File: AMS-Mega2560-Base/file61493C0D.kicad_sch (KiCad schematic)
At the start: 40 parts, among them IC10 LM2597MX-ADJ_NOPB, IC11 LM2597M-3.3_NOPB, IC12 OPA2340PA, IC9 LM2670SX-5.0_NOPB, J21 Screw_Terminal_01x02, J22 Conn_01x06, Q6 IRF9Z34NPBF, U1 BK_HTC-15M, U2 TL431LP

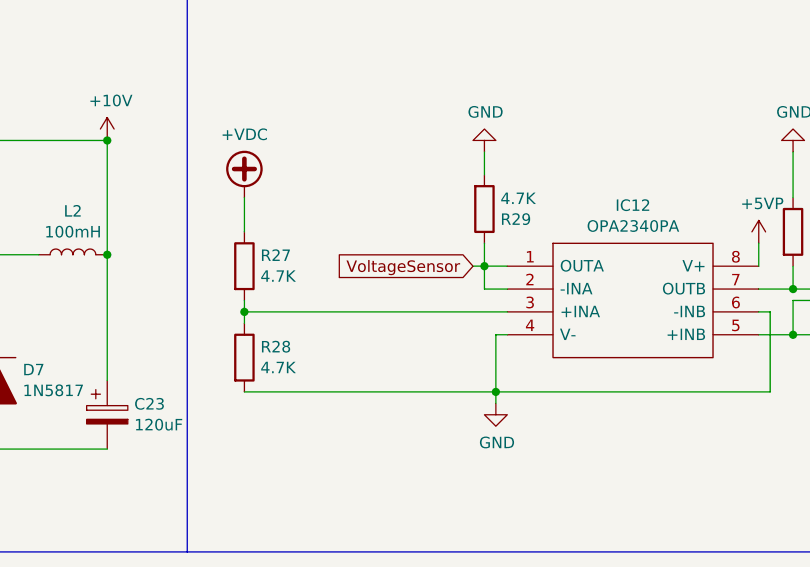
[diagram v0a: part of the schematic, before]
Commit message: slowly working on getting the board laid out and updates to some of the schematics.
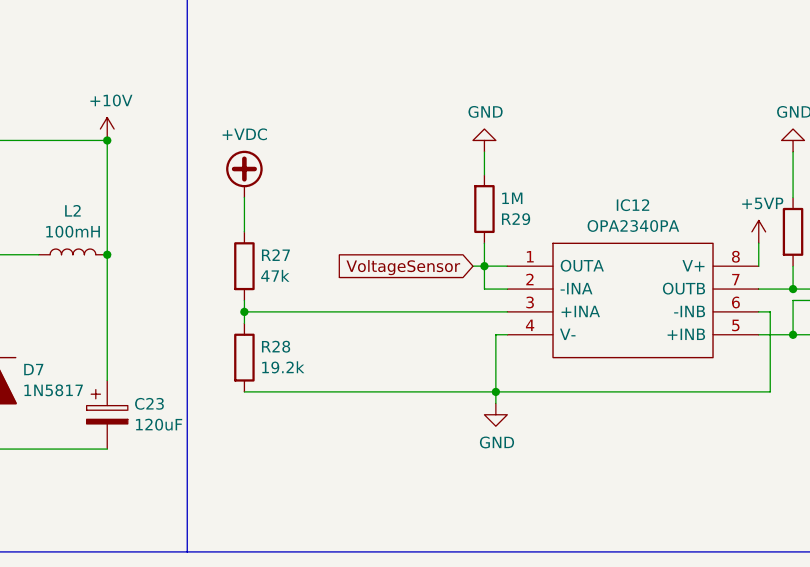
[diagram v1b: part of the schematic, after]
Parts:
- R27: value 4.7K -> 47k
- R28: value 4.7K -> 19.2k
- R29: value 4.7K -> 1M
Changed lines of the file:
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@@
       (effects (font (size 1.27 1.27)) (justify left))
     )
-    (property "Value" "4.7K" (id 1) (at 208.788 63.373 0)
+    (property "Value" "47k" (id 1) (at 208.788 63.373 0)
       (effects (font (size 1.27 1.27)) (justify left))
     )
@@
       (effects (font (size 1.27 1.27)) (justify left))
     )
-    (property "Value" "4.7K" (id 1) (at 208.788 73.533 0)
+    (property "Value" "19.2k" (id 1) (at 208.788 73.533 0)
       (effects (font (size 1.27 1.27)) (justify left))
     )
@@
       (effects (font (size 1.27 1.27)) (justify left))
     )
-    (property "Value" "4.7K" (id 1) (at 235.458 54.737 0)
+    (property "Value" "1M" (id 1) (at 235.458 54.737 0)
       (effects (font (size 1.27 1.27)) (justify left))
     )

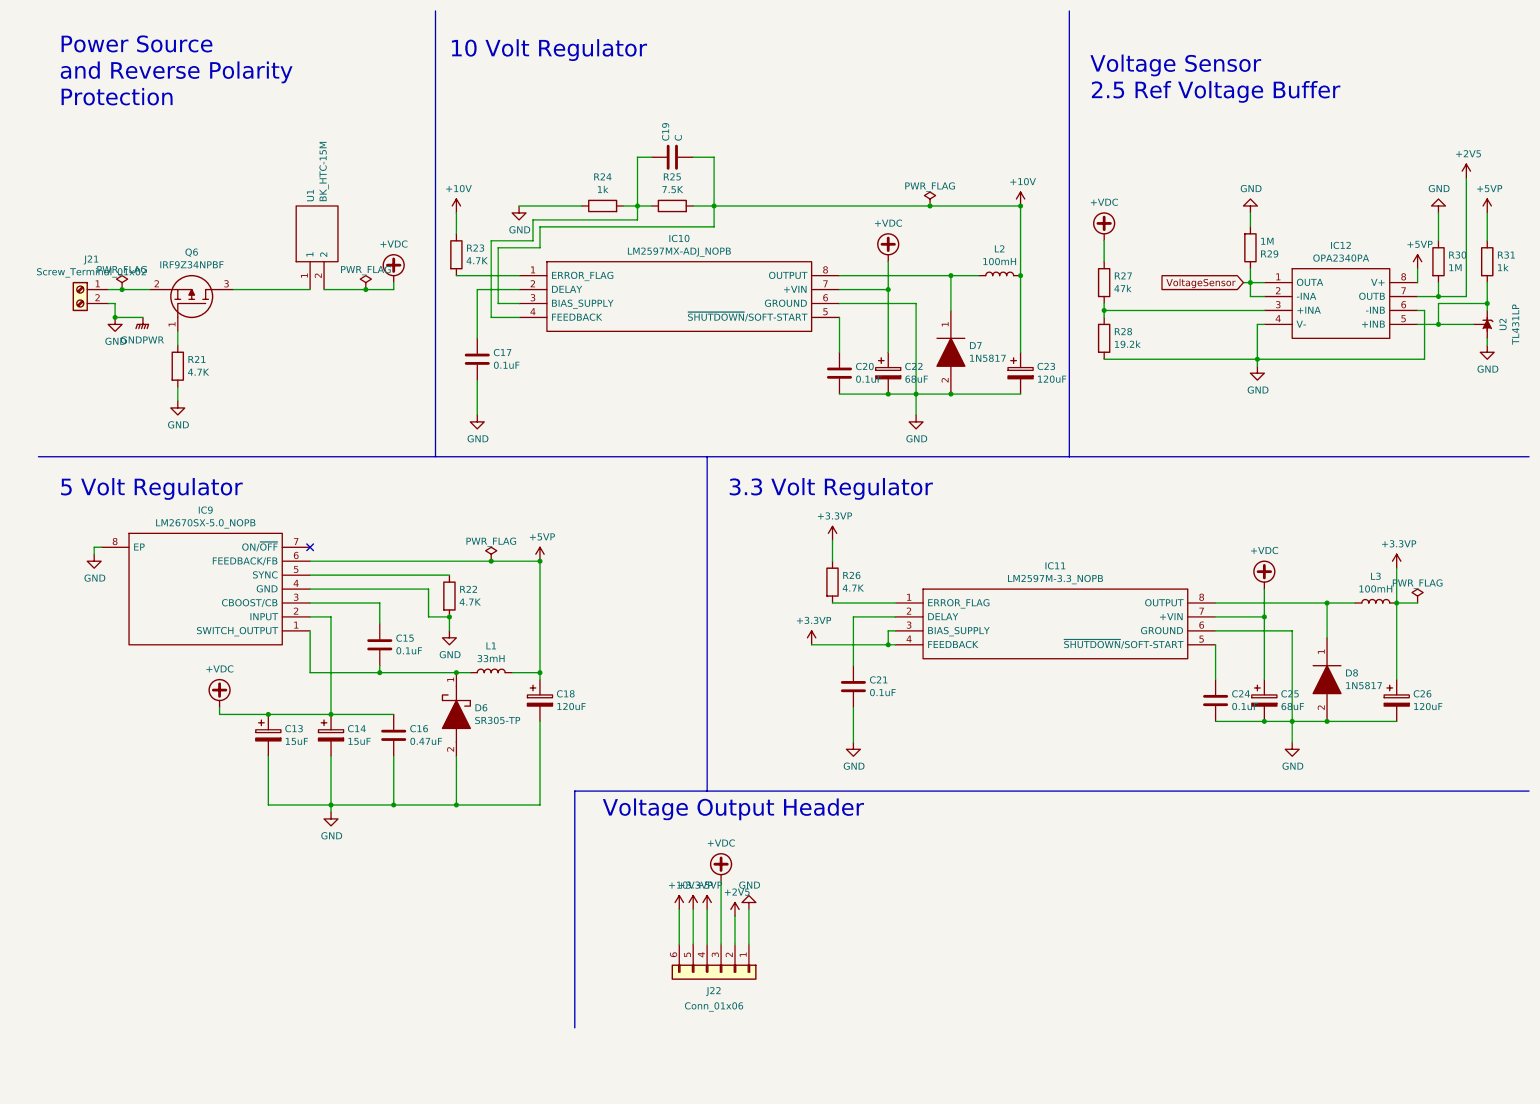
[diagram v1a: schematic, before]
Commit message: WIP for power on input and RTC battery switch over.
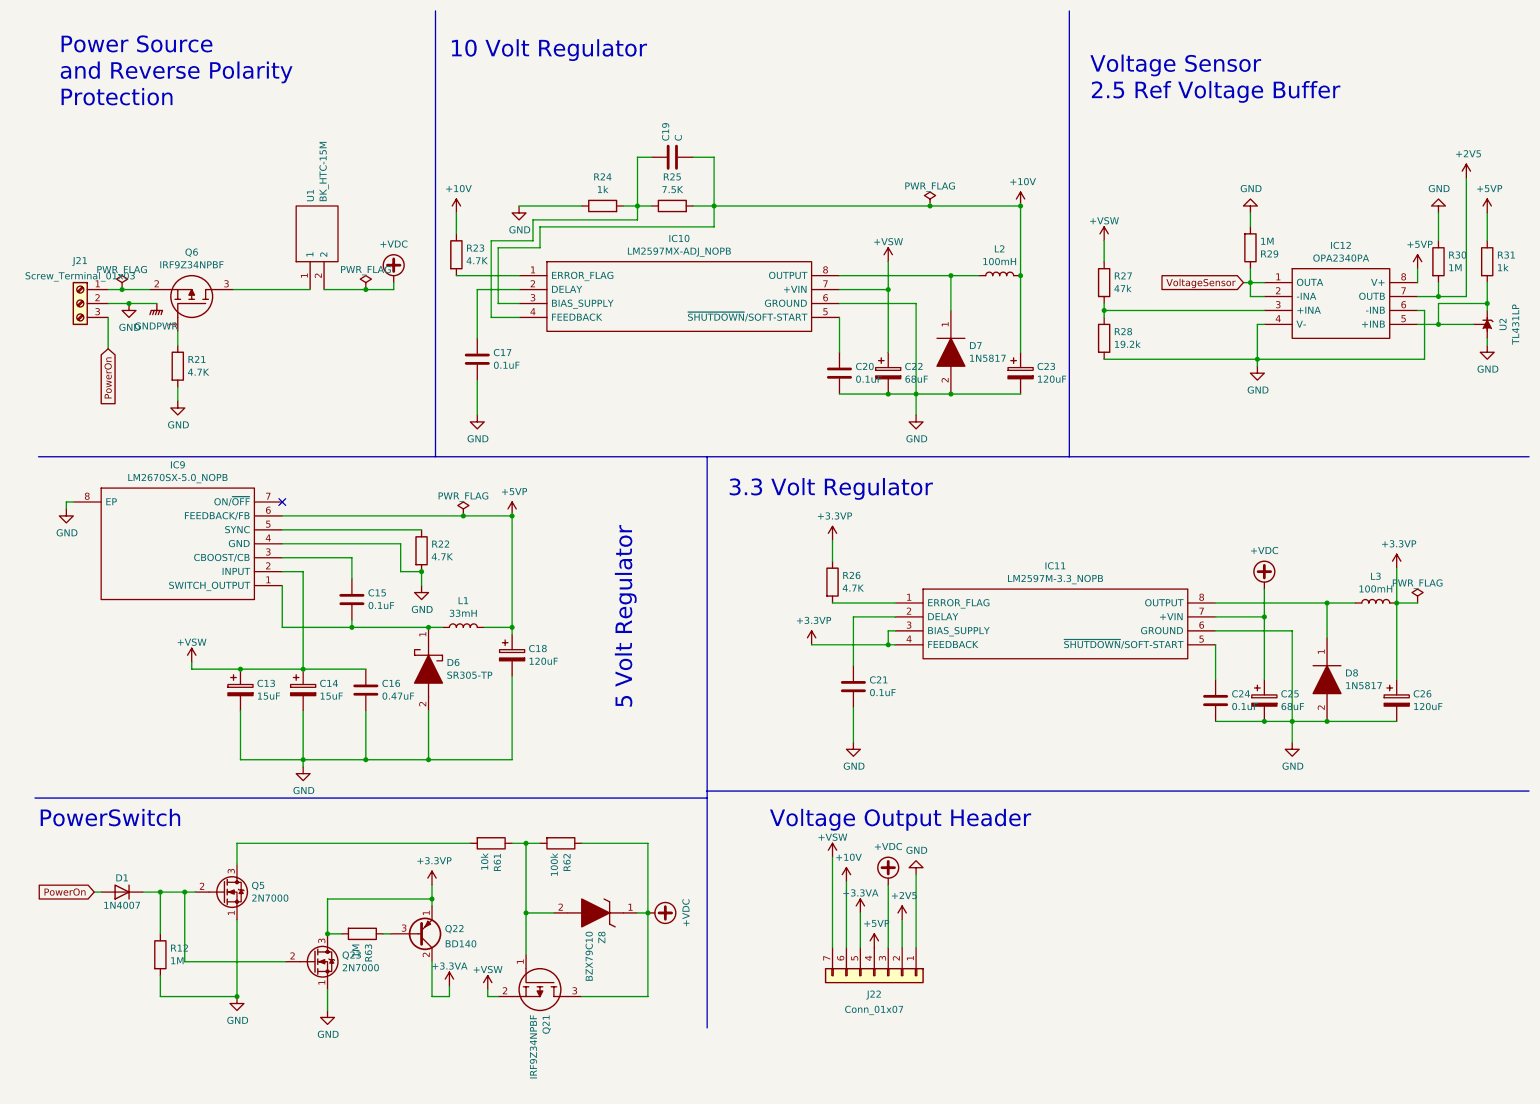
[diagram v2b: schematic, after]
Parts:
- removed J21: Screw_Terminal_01x02, TerminalBlock_Phoenix:TerminalBlock_Phoenix_MKDS-1,5-2-5.08_1x02_P5.08mm_Horizontal, symbol Connector:Screw_Terminal_01x02
- removed J22: Conn_01x06, Connector_PinHeader_2.54mm:PinHeader_1x06_P2.54mm_Vertical, symbol Connector_Generic:Conn_01x06
- added D1: 1N4007, Diode_THT:D_DO-41_SOD81_P10.16mm_Horizontal, symbol Diode:1N4007
- added J21: Screw_Terminal_01x03, TerminalBlock_Phoenix:TerminalBlock_Phoenix_MKDS-3-3-5.08_1x03_P5.08mm_Horizontal, symbol Connector:Screw_Terminal_01x03
- added J22: Conn_01x07, Connector_PinHeader_2.54mm:PinHeader_1x07_P2.54mm_Vertical, symbol Connector_Generic:Conn_01x07
- added Q21: IRF9Z34NPBF, SamacSys_Parts:TO254P469X1042X1967-3P, symbol SamacSys_Parts:IRF9Z34NPBF
- added Q22: BD140, Package_TO_SOT_THT:TO-126-3_Vertical, symbol Transistor_BJT:BD140
- added Q23, Q5: 2N7000, Package_TO_SOT_THT:TO-92_Inline, symbol Transistor_FET:2N7000
- added R12, R63: 1M, Resistor_THT:R_Axial_DIN0207_L6.3mm_D2.5mm_P2.54mm_Vertical, symbol Device:R
- added R61: 10k, Resistor_THT:R_Axial_DIN0207_L6.3mm_D2.5mm_P2.54mm_Vertical, symbol Device:R
- added R62: 100k, Resistor_THT:R_Axial_DIN0207_L6.3mm_D2.5mm_P2.54mm_Vertical, symbol Device:R
- added Z8: BZX79C10, SamacSys_Parts:DIOAD1068W53L380D172, symbol SamacSys_Parts:BZX79C10
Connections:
- net +10V: now also J22.6 (Pin_6)
- net +2V5: now also J22.2 (Pin_2)
- net +3.3VP: now also Q22.1 (E), Q23.3 (D), R63.2
- net +5VP: now also J22.4 (Pin_4)
- net +VDC: now also J22.3 (Pin_3), Q21.3, R62.1, Z8.1; no longer C13.1, C14.1, C16.1, C22.1, IC10.7 (+VIN), IC9.2 (INPUT), R27.1
- net GND: now also J21.2 (Pin_2), J22.1 (Pin_1), Q23.1 (S), Q5.1 (S), R12.2
- net at Q6.2: now also J21.1 (Pin_1)
- new net: D1.1 (K), Q23.2 (G), Q5.2 (G), R12.1
- new net: Q5.3 (D), R61.2
- new net: Q22.3 (B), R63.1
- new net: Q21.1, R61.1, R62.2, Z8.2
- new net +3.3VA: J22.5 (Pin_5), Q22.2 (C)
- new net +VSW: C13.1, C14.1, C16.1, C22.1, IC10.7 (+VIN), IC9.2 (INPUT), J22.7 (Pin_7), Q21.2, R27.1
- new net PowerOn: D1.2 (A), J21.3 (Pin_3)
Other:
- note added: "PowerSwitch"
- moved on the sheet: C13, C14, C15, C16, C18, D6, IC9, L1, R22

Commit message: fixing the 5V lines and removing the 5V fromt he MCU board and only using the 3Amp 5v power supplied by CampKeen
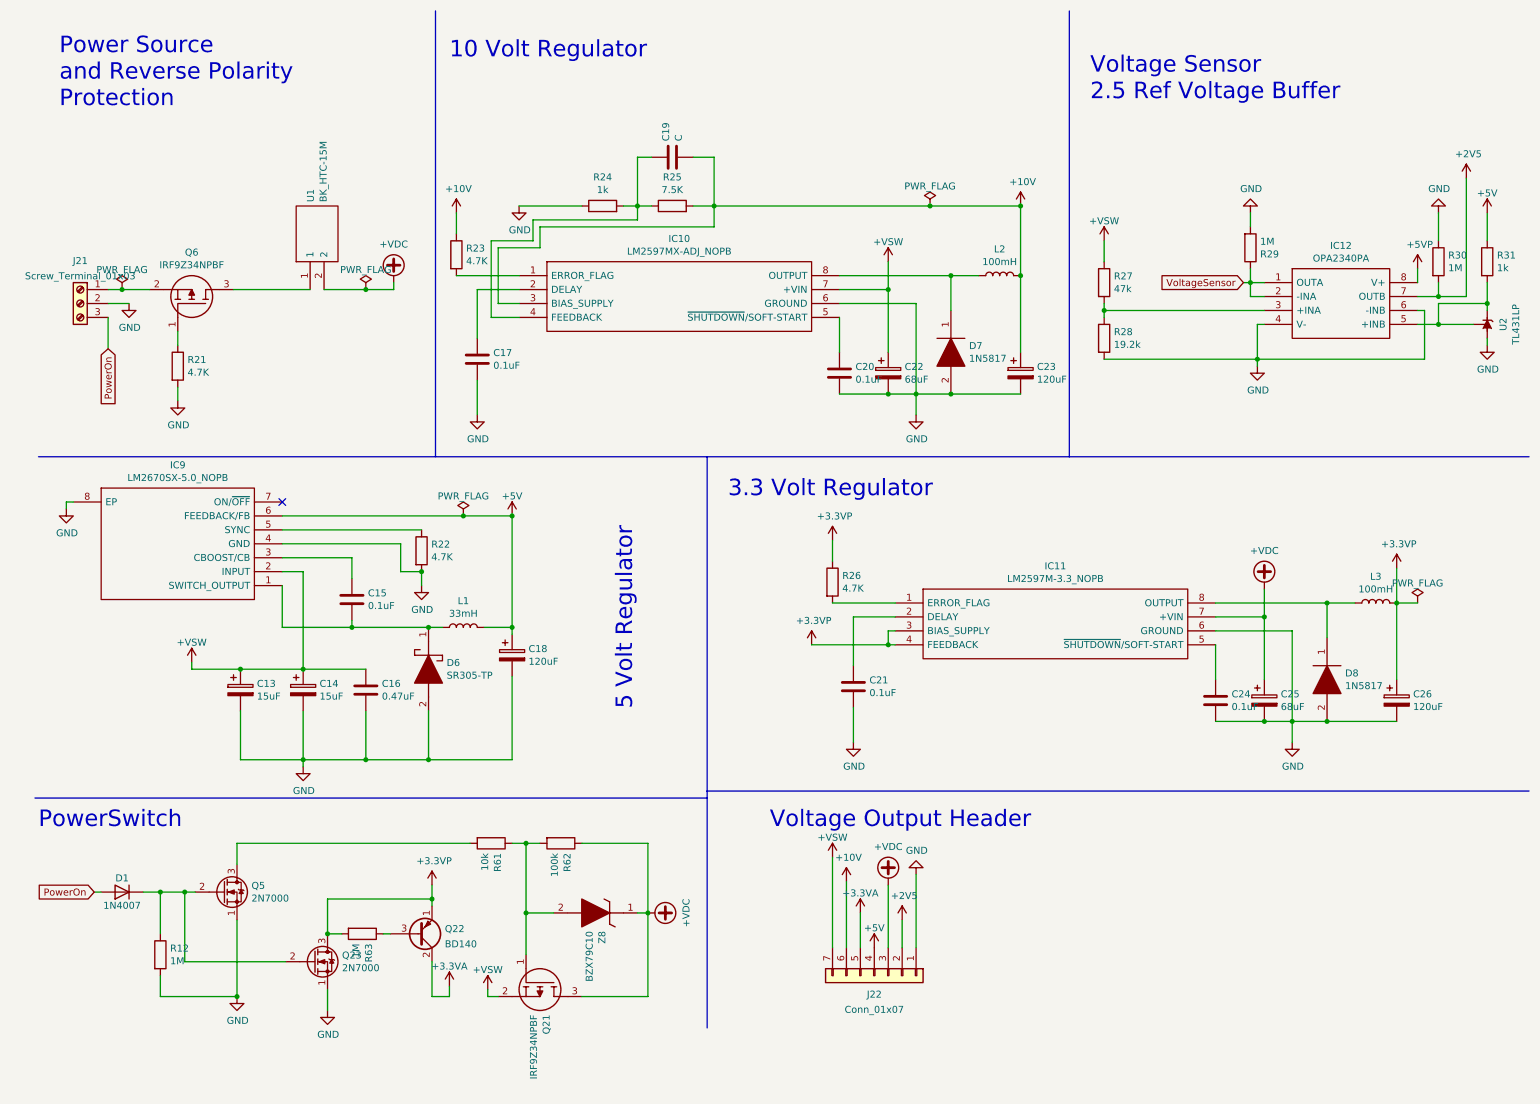
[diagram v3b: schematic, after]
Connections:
- net +5VP: no longer C18.1, IC9.6 (FEEDBACK/FB), J22.4 (Pin_4), L1.2, R31.1
- new net +5V: C18.1, IC9.6 (FEEDBACK/FB), J22.4 (Pin_4), L1.2, R31.1
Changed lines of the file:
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@@
 (kicad_sch (version 20211123) (generator eeschema)
   (paper "A4")
-  (junction (at 29.21 66.04) (diameter 0) (color 0 0 0 0)
-  )
   (junction (at 236.22 142.24) (diameter 0) (color 0 0 0 0)
   )
@@
   (junction (at 69.85 125.095) (diameter 0) (color 0 0 0 0)
   )
+  (junction (at 99.06 104.775) (diameter 0) (color 0 0 0 0)
+  )
   (junction (at 233.68 62.23) (diameter 0) (color 0 0 0 0)
   )
@@
   )
   (junction (at 101.6 164.465) (diameter 0) (color 0 0 0 0)
-  )
-  (junction (at 99.06 104.775) (diameter 0) (color 0 0 0 0)
   )
   (junction (at 60.96 149.225) (diameter 0) (color 0 0 0 0)
@@
   )
   (wire (pts (xy 168.91 120.65) (xy 157.48 120.65))
-    (stroke (width 0) (type default) (color 0 0 0 0))
-  )
-  (wire (pts (xy 29.21 66.04) (xy 34.29 66.04))
     (stroke (width 0) (type default) (color 0 0 0 0))
   )
@@
     (pin "2")
   )
-  (symbol (lib_id "power:+5VP") (at 99.06 104.775 0) (unit 1)
-    (in_bom yes) (on_board yes)
-    (property "Reference" "#PWR064" (id 0) (at 99.06 108.585 0)
-      (effects (font (size 1.27 1.27)) hide)
-    )
-    (property "Value" "+5VP" (id 1) (at 99.441 100.3808 0))
-    (property "Footprint" "" (id 2) (at 99.06 104.775 0)
-      (effects (font (size 1.27 1.27)) hide)
-    )
-    (property "Datasheet" "" (id 3) (at 99.06 104.775 0)
-      (effects (font (size 1.27 1.27)) hide)
-    )
-    (pin "1")
-  )
   (symbol (lib_id "power:GND") (at 172.72 170.18 0) (mirror x) (unit 1)
     (in_bom yes) (on_board yes)
@@
     )
     (property "Datasheet" "" (id 3) (at 172.72 170.18 0)
-      (effects (font (size 1.27 1.27)) hide)
-    )
-    (pin "1")
-  )
-  (symbol (lib_id "power:+5VP") (at 165.1 183.515 0) (unit 1)
-    (in_bom yes) (on_board yes)
-    (property "Reference" "#PWR067" (id 0) (at 165.1 187.325 0)
-      (effects (font (size 1.27 1.27)) hide)
-    )
-    (property "Value" "+5VP" (id 1) (at 165.481 179.1208 0))
-    (property "Footprint" "" (id 2) (at 165.1 183.515 0)
-      (effects (font (size 1.27 1.27)) hide)
-    )
-    (property "Datasheet" "" (id 3) (at 165.1 183.515 0)
       (effects (font (size 1.27 1.27)) hide)
     )
@@
     (pin "1")
   )
-  (symbol (lib_id "power:+5VP") (at 276.86 49.53 0) (unit 1)
-    (in_bom yes) (on_board yes)
-    (property "Reference" "#PWR085" (id 0) (at 276.86 53.34 0)
-      (effects (font (size 1.27 1.27)) hide)
-    )
-    (property "Value" "+5VP" (id 1) (at 277.241 45.1358 0))
-    (property "Footprint" "" (id 2) (at 276.86 49.53 0)
-      (effects (font (size 1.27 1.27)) hide)
-    )
-    (property "Datasheet" "" (id 3) (at 276.86 49.53 0)
-      (effects (font (size 1.27 1.27)) hide)
-    )
-    (pin "1")
-  )
   (symbol (lib_id "Device:R") (at 267.97 58.42 0) (unit 1)
     (in_bom yes) (on_board yes)
@@
     (pin "1")
   )
+  (symbol (lib_id "power:+5V") (at 165.1 183.515 0) (unit 1)
+    (in_bom yes) (on_board yes) (fields_autoplaced)
+    (property "Reference" "#PWR?" (id 0) (at 165.1 187.325 0)
+      (effects (font (size 1.27 1.27)) hide)
+    )
+    (property "Value" "+5V" (id 1) (at 165.1 179.9105 0))
+    (property "Footprint" "" (id 2) (at 165.1 183.515 0)
+      (effects (font (size 1.27 1.27)) hide)
+    )
+    (property "Datasheet" "" (id 3) (at 165.1 183.515 0)
+      (effects (font (size 1.27 1.27)) hide)
+    )
+    (pin "1")
+  )
   (symbol (lib_id "Device:R") (at 34.925 184.785 0) (unit 1)
     (in_bom yes) (on_board yes)
@@
     (pin "2")
   )
-  (symbol (lib_id "power:GNDPWR") (at 34.29 66.04 0) (unit 1)
-    (in_bom yes) (on_board yes) (fields_autoplaced)
-    (property "Reference" "#PWR055" (id 0) (at 34.29 71.12 0)
-      (effects (font (size 1.27 1.27)) hide)
-    )
-    (property "Value" "GNDPWR" (id 1) (at 34.163 70.1961 0))
-    (property "Footprint" "" (id 2) (at 34.29 67.31 0)
-      (effects (font (size 1.27 1.27)) hide)
-    )
-    (property "Datasheet" "" (id 3) (at 34.29 67.31 0)
-      (effects (font (size 1.27 1.27)) hide)
-    )
-    (pin "1")
-  )
   (symbol (lib_id "power:PWR_FLAG") (at 27.94 63.5 0) (unit 1)
     (in_bom yes) (on_board yes) (fields_autoplaced)
@@
       (effects (font (size 1.27 1.27)) hide)
     )
+    (pin "1")
+  )
+  (symbol (lib_id "power:+5V") (at 99.06 104.775 0) (unit 1)
+    (in_bom yes) (on_board yes) (fields_autoplaced)
+    (property "Reference" "#PWR?" (id 0) (at 99.06 108.585 0)
+      (effects (font (size 1.27 1.27)) hide)
+    )
+    (property "Value" "+5V" (id 1) (at 99.06 101.1705 0))
+    (property "Footprint" "" (id 2) (at 99.06 104.775 0)
+      (effects (font (size 1.27 1.27)) hide)
+    )
+    (property "Datasheet" "" (id 3) (at 99.06 104.775 0)
+      (effects (font (size 1.27 1.27)) hide)
+    )
+    (pin "1")
+  )
+  (symbol (lib_id "power:+5V") (at 276.86 49.53 0) (unit 1)
+    (in_bom yes) (on_board yes) (fields_autoplaced)
+    (property "Reference" "#PWR?" (id 0) (at 276.86 53.34 0)
+      (effects (font (size 1.27 1.27)) hide)
+    )
+    (property "Value" "+5V" (id 1) (at 276.86 45.9255 0))
+    (property "Footprint" "" (id 2) (at 276.86 49.53 0)
+      (effects (font (size 1.27 1.27)) hide)
+    )
+    (property "Datasheet" "" (id 3) (at 276.86 49.53 0)
+      (effects (font (size 1.27 1.27)) hide)
+    )
